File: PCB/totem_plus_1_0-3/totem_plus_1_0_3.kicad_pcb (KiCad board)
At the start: 2 copper layers, 264.6 x 94.4 mm, 108 parts, among them J1 MJ-4PP-9, J2 MJ-4PP-9, U1 xiao-ble, U2 xiao-ble

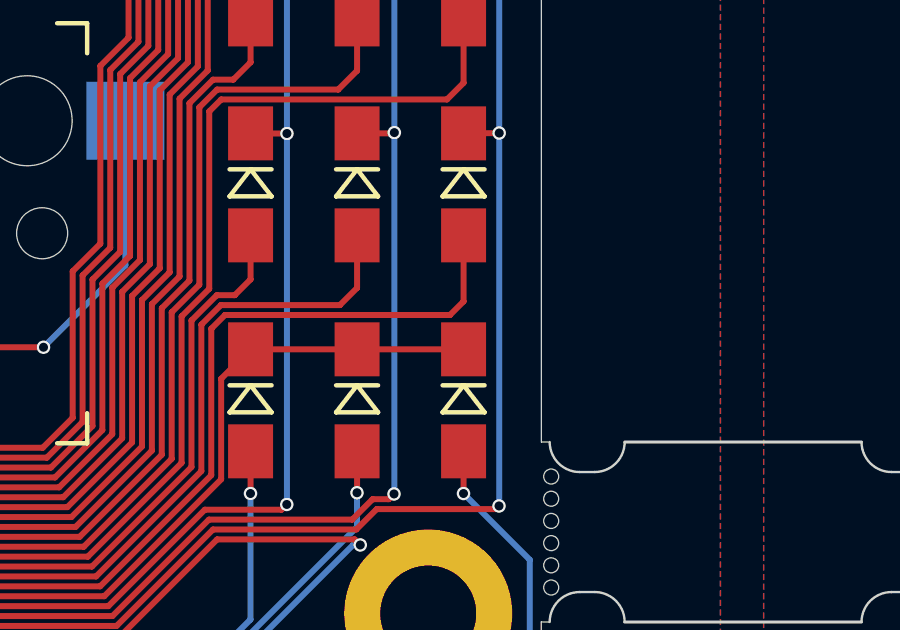
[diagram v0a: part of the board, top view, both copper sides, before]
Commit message: Added case, updated README
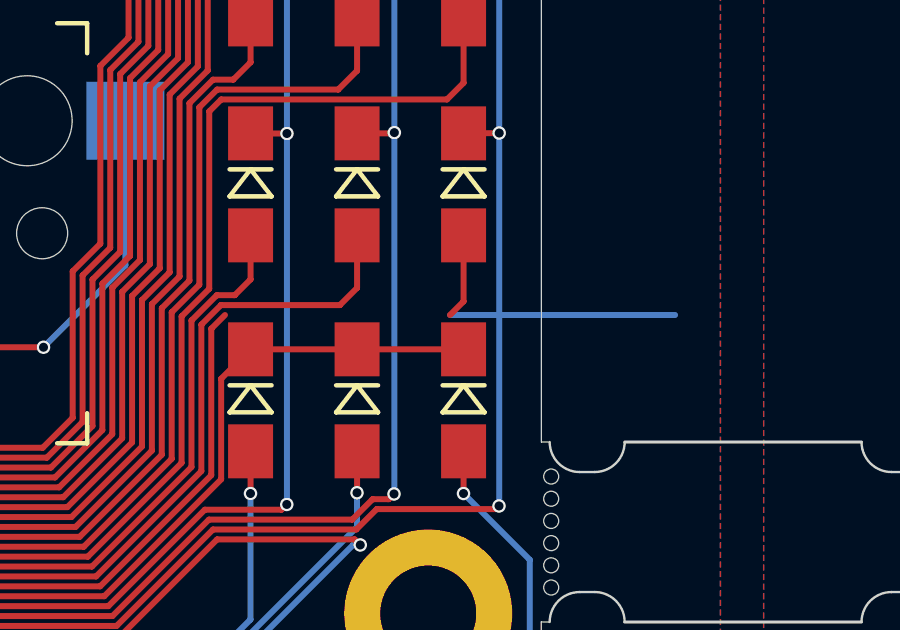
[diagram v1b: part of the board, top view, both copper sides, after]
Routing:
- net ROW0_L: track 229.3 -> 236.8 mm
- net Net-(DL1-A): track 181.5 -> 174.0 mm
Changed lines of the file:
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@@
 	(paper "User" 299.999 200)
 	(title_block
-		(title "TOTEM split keyboard")
-		(date "2022-11-03")
+		(title "TOTEM Plus 1 split keyboard")
+		(date "2024-09-20")
 		(rev "0.3")
-		(comment 1 "Made by GEIST")
+		(comment 1 "Modified by Atila M Schrieber")
+		(comment 2 "Made by GEIST")
 	)
 	(layers
@@
 		)
 		(property "Value" "SW_SPDT"
-			(at 2.25 9.2 360)
+			(at 2.25 9.2 0)
 			(layer "F.Fab")
 			(effects
@@
 		)
 		(property "Footprint" "TOTEMlib:MSK12C02"
-			(at 0 0 360)
+			(at 0 0 0)
 			(layer "F.Fab")
 			(hide yes)
@@
 		)
 		(property "Datasheet" ""
-			(at 0 0 360)
+			(at 0 0 0)
 			(layer "F.Fab")
 			(hide yes)
@@
 		)
 		(property "Description" ""
-			(at 0 0 360)
+			(at 0 0 0)
 			(layer "F.Fab")
 			(hide yes)
@@
 	)
 	(segment
+		(start 140.225 102.05)
+		(end 147.725 102.05)
+		(width 0.2)
+		(layer "B.Cu")
+		(net 1)
+	)
+	(segment
 		(start 29.452565 86.039348)
 		(end 30.672565 84.819348)
@@
 		(width 0.2)
 		(layer "F.Cu")
-		(net 2)
-	)
-	(segment
-		(start 140.225 102.05)
-		(end 132.725 102.05)
-		(width 0.2)
-		(layer "F.Cu")
